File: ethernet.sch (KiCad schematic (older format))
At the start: 31 parts, among them J2 08B0-1X1T-36-F, U6 DP83848JSQ_NOPB, Y1 ABM8G-25.000MHZ-18-D2Y-T

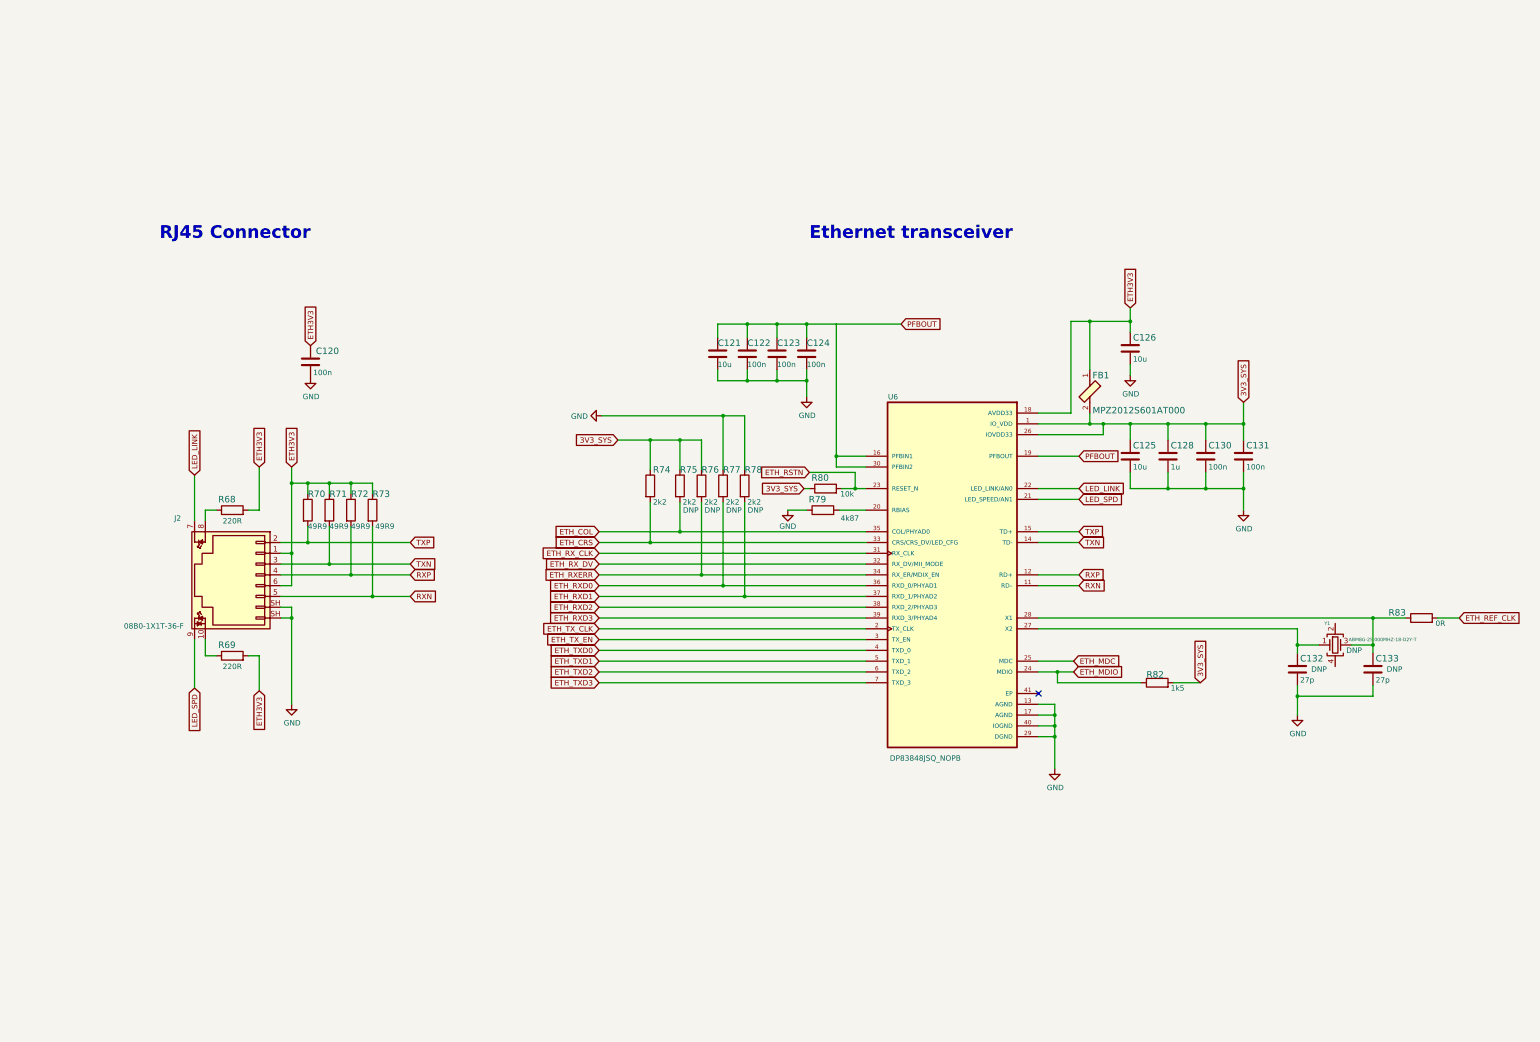
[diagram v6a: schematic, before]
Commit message: Change ETH PHY to KSZ9031RNXCA supporting 1GbE
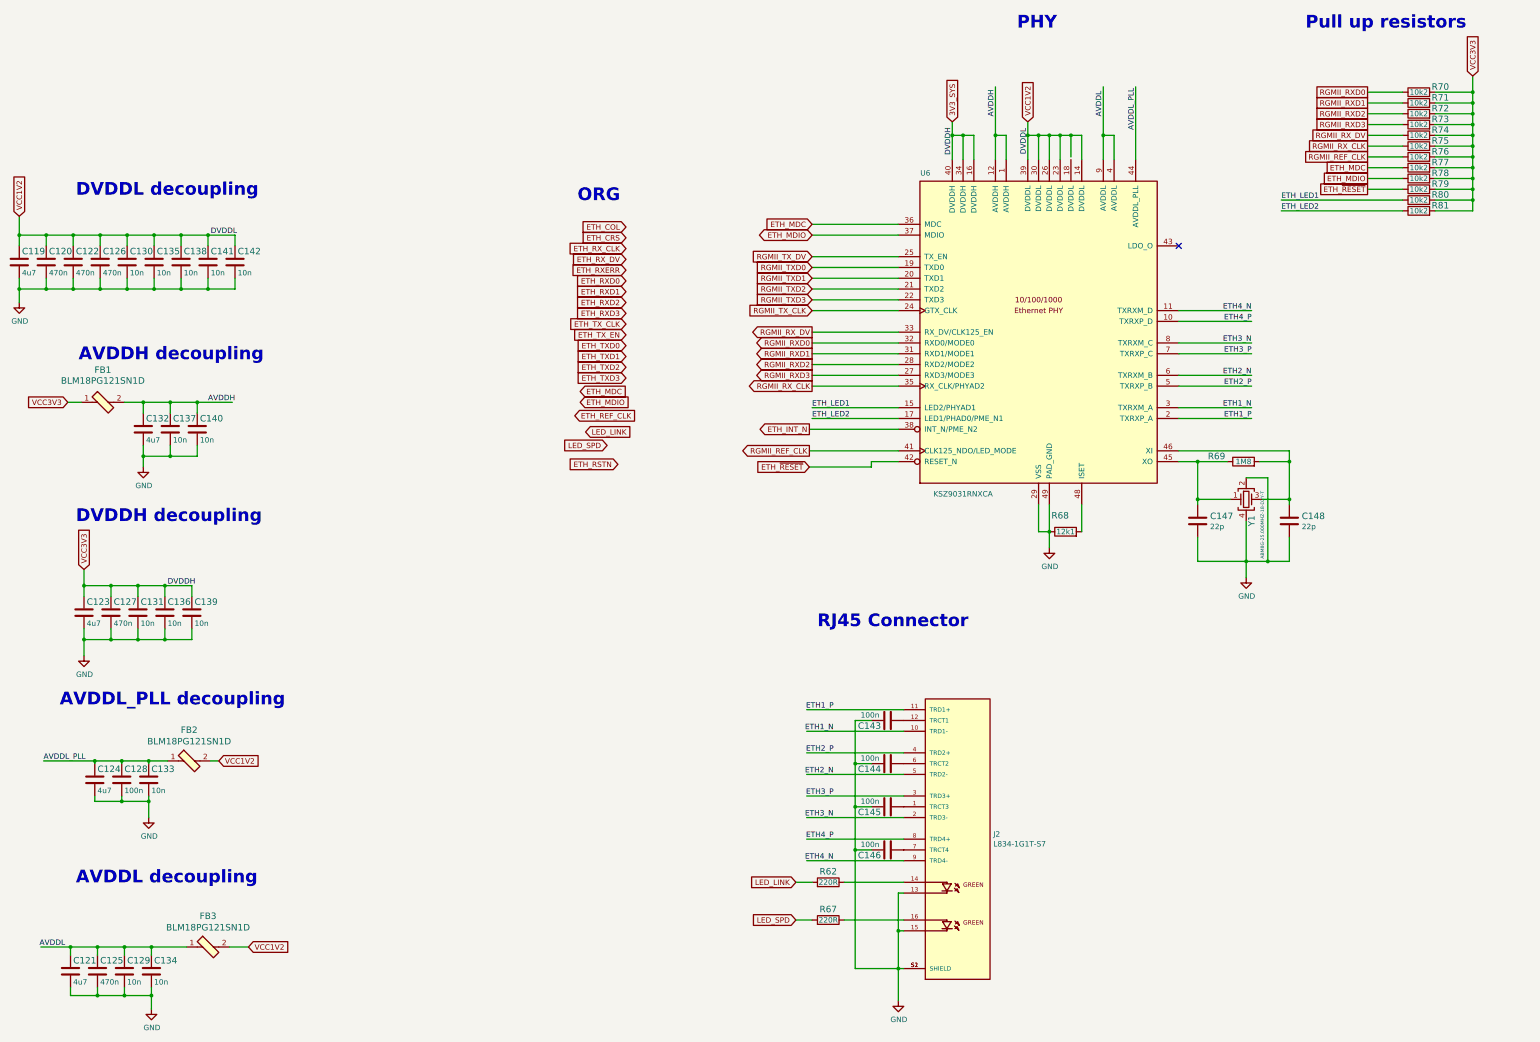
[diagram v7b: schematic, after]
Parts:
- removed C120, C122, C123, C124, C130, C131: C_100n_0402_6V3, lpddr4-test-board-footprints:0402-cap, symbol lpddr4-test-board:C_100n_0402_6V3
- removed C121, C125, C126: C_10u_0603, lpddr4-test-board-footprints:0603-cap, symbol lpddr4-test-board:C_10u_0603
- removed C128: C_1u_0402, lpddr4-test-board-footprints:0402-cap, symbol lpddr4-test-board:C_1u_0402
- removed C132, C133: C_27p_0402, lpddr4-test-board-footprints:0402-cap, symbol lpddr4-test-board:C_27p_0402
- removed FB1: MPZ2012S601AT000, lpddr4-test-board-footprints:0805-res, symbol lpddr4-test-board:MPZ2012S601AT000
- removed J2: 08B0-1X1T-36-F, lpddr4-test-board-footprints:BEL_08B0-1X1T-36-F, symbol lpddr4-test-board:08B0-1X1T-36-F
- removed R68, R69: R_220R_0402, lpddr4-test-board-footprints:0402-res, symbol lpddr4-test-board:R_220R_0402
- removed R70, R71, R72, R73: R_49R9_0402, lpddr4-test-board-footprints:0402-res, symbol lpddr4-test-board:R_49R9_0402
- removed R74, R75, R76, R77, R78: R_2k2_0402, lpddr4-test-board-footprints:0402-res, symbol lpddr4-test-board:R_2k2_0402
- removed R79: R_4k87_0402, lpddr4-test-board-footprints:0402-res, symbol lpddr4-test-board:R_4k87_0402
- removed R80: R_10k_0402, lpddr4-test-board-footprints:0402-res, symbol lpddr4-test-board:R_10k_0402
- removed R82: R_1k5_0402, lpddr4-test-board-footprints:0402-res, symbol lpddr4-test-board:R_1k5_0402
- removed R83: R_0R_0402, lpddr4-test-board-footprints:0402-res, symbol lpddr4-test-board:R_0R_0402
- removed U6: DP83848JSQ_NOPB, lpddr4-test-board-footprints:DP83848JSQ-NOPB, symbol lpddr4-test-board:DP83848JSQ_NOPB
- added C119, C121, C123, C124, C132: C_4u7_0402, artix-dc-scm-footprints:0402-cap, symbol lpddr4-test-board:C_4u7_0402
- added C120, C125, C127: C_470n_0402, artix-dc-scm-footprints:0402-cap, symbol lpddr4-test-board:C_470n_0402
- added C122, C126: C_470n_0402, artix-dc-scm-footprints:0402-cap, symbol antmicroCapacitors0402:C_470n_0402
- added C128, C143, C144, C145, C146: C_100n_0402, artix-dc-scm-footprints:0402-cap, symbol lpddr4-test-board:C_100n_0402_16V
- added C129, C131, C133, C134, C136, C139: C_10n_0402, artix-dc-scm-footprints:0402-cap, symbol lpddr4-test-board:C_10n_0402
- added C130: C_10n_0402, artix-dc-scm-footprints:0402-cap, symbol antmicroCapacitors0402:C_470n_0402
- added C135, C138, C141, C142: C_10n_0402, artix-dc-scm-footprints:0402-cap, symbol antmicroCapacitors0402:C_10n_0402
- added C137: C_10n_0402, artix-dc-scm-footprints:0402-cap, symbol lpddr4-test-board:C_4u7_0402
- added C140: C_10n_0402, artix-dc-scm-footprints:0402-cap, symbol antmicroCapacitors0402:C_4u7_0402
- added C147, C148: C_22p_0402, artix-dc-scm-footprints:0402-cap, symbol antmicroCapacitors0402:C_22p_0402
- added FB1, FB2, FB3: BLM18PG121SN1D, artix-dc-scm-footprints:0603-res, symbol antmicroFerriteBeadsandChips:BLM18PG121SN1D
- added J2: L834-1G1T-S7, artix-dc-scm-footprints:BEL_L834-1G1T-S7, symbol antmicroModularConnectorsJacksWithMagnetics:L834-1G1T-S7
- added R62, R67: R_220R_0402, artix-dc-scm-footprints:0402-res, symbol lpddr4-test-board:R_220R_0402
- added R68: R_12k1_0402, artix-dc-scm-footprints:0402-res, symbol antmicroResistors0402:R_12k1_0402
- added R69: R_1M8_0402, artix-dc-scm-footprints:0402-res, symbol antmicroResistors0402:R_1M8_0402
- added R70, R71, R72, R73, R74, R75, R76, R77, R78, R79, R80, R81: R_10k2_0402, lpddr4-test-board-footprints:0402-res, symbol lpddr4-test-board:R_10k2_0402
- added U6: KSZ9031RNXCA, artix-dc-scm-footprints:QFN-48-Microchip-QFN77-48LD-PL-2, symbol antmicroInterfaceControllers:KSZ9031RNXCA
- Y1: footprint lpddr4-test-board-footprints:KX-7 -> artix-dc-scm-footprints:KX-7; Populate DNP -> (none)
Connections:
- net labels added: AVDDH, AVDDL, AVDDL_PLL, DVDDH, DVDDL, ETH1_N, ETH1_P, ETH2_N, ETH2_P, ETH3_N, ETH3_P, ETH4_N, ETH4_P, ETH_INT_N, ETH_LED1, ETH_LED2, ETH_~RESET, RGMII_REF_CLK, RGMII_RXD0, RGMII_RXD1, RGMII_RXD2, RGMII_RXD3, RGMII_RX_CLK, RGMII_RX_DV, RGMII_TXD0, RGMII_TXD1, RGMII_TXD2, RGMII_TXD3, RGMII_TX_CLK, RGMII_TX_DV, VCC1V2, VCC3V3
- net labels removed: ETH3V3, PFBOUT, RXN, RXP, TXN, TXP
- wire segments 167 -> 246
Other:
- note added: "AVDDH decoupling"
- note added: "AVDDL decoupling"
- note added: "AVDDL_PLL decoupling"
- note added: "DVDDH decoupling"
- note added: "DVDDL decoupling"
- note added: "ORG"
- note added: "PHY"
- note added: "Pull up resistors"
- note removed: "Ethernet transceiver"

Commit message: Connect new PHY signals
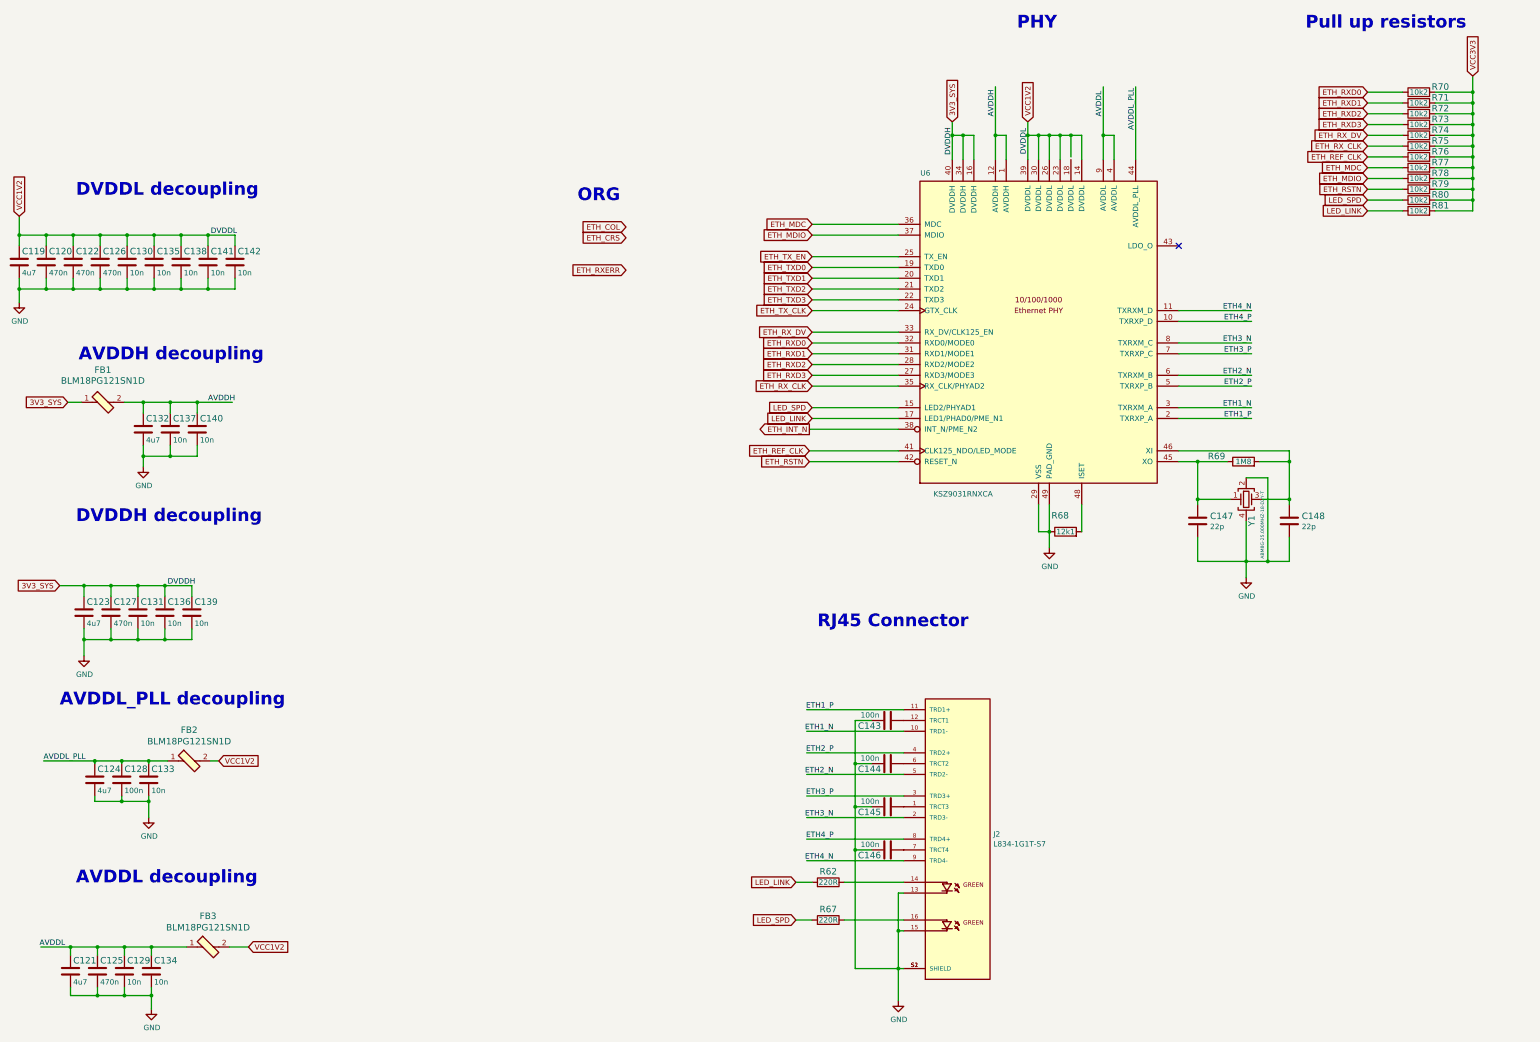
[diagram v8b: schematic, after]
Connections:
- net labels removed: ETH_LED1, ETH_LED2, ETH_~RESET, RGMII_REF_CLK, RGMII_RXD0, RGMII_RXD1, RGMII_RXD2, RGMII_RXD3, RGMII_RX_CLK, RGMII_RX_DV, RGMII_TXD0, RGMII_TXD1, RGMII_TXD2, RGMII_TXD3, RGMII_TX_CLK, RGMII_TX_DV
- wire segments 246 -> 244
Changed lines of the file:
@@
 Wire Wire Line
 	8775 4650 9575 4650
-Text Label 8775 4650 0    50   ~ 0
-ETH_LED1
-Text Label 8775 4750 0    50   ~ 0
-ETH_LED2
 Wire Wire Line
 	9575 4750 8775 4750
@@
 	11275 5550 11275 5800
 NoConn ~ 12175 3150
-Text GLabel 8750 5200 0    50   Input ~ 0
-ETH_~RESET
-Wire Wire Line
-	9575 5150 9325 5150
 Wire Wire Line
 	8750 5050 9575 5050
@@
 Text GLabel 8750 4850 0    50   Output ~ 0
 ETH_INT_N
-Text GLabel 8750 5050 0    50   Output ~ 0
-RGMII_REF_CLK
-Wire Wire Line
-	9325 5150 9325 5200
-Wire Wire Line
-	9325 5200 8750 5200
-Text GLabel 8775 4450 0    50   Output ~ 0
-RGMII_RX_CLK
-Text GLabel 8775 4350 0    50   Output ~ 0
-RGMII_RXD3
-Text GLabel 8775 4250 0    50   Output ~ 0
-RGMII_RXD2
-Text GLabel 8775 4150 0    50   Output ~ 0
-RGMII_RXD1
-Text GLabel 8775 4050 0    50   Output ~ 0
-RGMII_RXD0
 Wire Wire Line
 	8775 4350 9575 4350
@@
 Wire Wire Line
 	9575 4050 8775 4050
-Text GLabel 8775 3750 0    50   Input ~ 0
-RGMII_TX_CLK
-Text GLabel 8775 3650 0    50   Input ~ 0
-RGMII_TXD3
-Text GLabel 8775 3550 0    50   Input ~ 0
-RGMII_TXD2
-Text GLabel 8775 3450 0    50   Input ~ 0
-RGMII_TXD1
-Text GLabel 8775 3350 0    50   Input ~ 0
-RGMII_TXD0
-Text GLabel 8775 3250 0    50   Input ~ 0
-RGMII_TX_DV
 Wire Wire Line
 	8775 3650 9575 3650
@@
 Wire Wire Line
 	9575 3350 8775 3350
-Text GLabel 8775 3050 0    50   BiDi ~ 0
-ETH_MDIO
-Text GLabel 8775 2950 0    50   Input ~ 0
-ETH_MDC
 Wire Wire Line
 	8775 2950 9575 2950
@@
 Wire Wire Line
 	10275 2125 10175 2125
-Text GLabel 8775 3950 0    50   Output ~ 0
-RGMII_RX_DV
 $Comp
 L antmicroInterfaceControllers:KSZ9031RNXCA U?
@@
 	1    0    0    -1
 $EndComp
-Text GLabel 13925 2125 0    50   UnSpc ~ 0
-RGMII_RX_DV
-Text GLabel 13925 2025 0    50   UnSpc ~ 0
-RGMII_RXD3
-Text GLabel 13925 1925 0    50   UnSpc ~ 0
-RGMII_RXD2
-Text GLabel 13925 1725 0    50   UnSpc ~ 0
-RGMII_RXD0
-Text GLabel 13925 1825 0    50   UnSpc ~ 0
-RGMII_RXD1
-Text GLabel 13925 2225 0    50   UnSpc ~ 0
-RGMII_RX_CLK
 Text GLabel 14900 1575 1    50   Input ~ 0
 VCC3V3
-Text GLabel 13925 2325 0    50   UnSpc ~ 0
-RGMII_REF_CLK
-Text GLabel 13925 2525 0    50   UnSpc ~ 0
-ETH_MDIO
-Text GLabel 13925 2425 0    50   UnSpc ~ 0
-ETH_MDC
-Text GLabel 13925 2625 0    50   UnSpc ~ 0
-ETH_~RESET
-Text Label 13125 2725 0    50   ~ 0
-ETH_LED1
-Text Label 13125 2825 0    50   ~ 0
-ETH_LED2
 Text Notes 13350 1150 0    118  ~ 24
 Pull up resistors
@@
 	13925 2625 14250 2625
 Wire Wire Line
-	14250 2725 13125 2725
-Wire Wire Line
-	13125 2825 14250 2825
-Text GLabel 7050 4075 0    50   Input ~ 0
+	14250 2725 13925 2725
+Wire Wire Line
+	13925 2825 14250 2825
+Text GLabel 8775 3350 0    50   Input ~ 0
 ETH_TXD0
-Text GLabel 7050 4175 0    50   Input ~ 0
+Text GLabel 8775 3450 0    50   Input ~ 0
 ETH_TXD1
-Text GLabel 7050 4275 0    50   Input ~ 0
+Text GLabel 8775 3550 0    50   Input ~ 0
 ETH_TXD2
-Text GLabel 7050 4375 0    50   Input ~ 0
+Text GLabel 8775 3650 0    50   Input ~ 0
 ETH_TXD3
-Text GLabel 7050 3875 0    50   Input ~ 0
+Text GLabel 8775 3750 0    50   Input ~ 0
 ETH_TX_CLK
-Text GLabel 7050 3975 0    50   Input ~ 0
+Text GLabel 8775 3250 0    50   Input ~ 0
 ETH_TX_EN
-Text GLabel 7050 3475 0    50   Input ~ 0
+Text GLabel 8775 4050 0    50   Input ~ 0
 ETH_RXD0
-Text GLabel 7050 3575 0    50   Input ~ 0
+Text GLabel 8775 4150 0    50   Input ~ 0
 ETH_RXD1
-Text GLabel 7050 3675 0    50   Input ~ 0
+Text GLabel 8775 4250 0    50   Input ~ 0
 ETH_RXD2
-Text GLabel 7050 3775 0    50   Input ~ 0
+Text GLabel 8775 4350 0    50   Input ~ 0
 ETH_RXD3
-Text GLabel 7050 3175 0    50   Input ~ 0
+Text GLabel 8775 4450 0    50   Input ~ 0
 ETH_RX_CLK
-Text GLabel 7050 3275 0    50   Input ~ 0
+Text GLabel 8775 3950 0    50   Input ~ 0
 ETH_RX_DV
 Text GLabel 7050 3375 0    50   Input ~ 0
@@
 Text GLabel 7050 3075 0    50   Input ~ 0
 ETH_CRS
-Text GLabel 6625 4500 2    50   Input ~ 0
+Text GLabel 8775 2950 0    50   Input ~ 0
 ETH_MDC
-Text GLabel 6625 4600 2    50   Input ~ 0
+Text GLabel 8775 3050 0    50   Input ~ 0
 ETH_MDIO
 Text Notes 6600 2750 0    118  ~ 24
@@
 Text GLabel 10075 2000 1    50   Input ~ 0
 3V3_SYS
-Text GLabel 6575 4725 2    50   Input ~ 0
+Text GLabel 8750 5050 0    50   Input ~ 0
 ETH_REF_CLK
-Text GLabel 6675 4875 2    50   Input ~ 0
+Text GLabel 8775 4750 0    50   Input ~ 0
 LED_LINK
-Text GLabel 6875 5000 0    50   Input ~ 0
+Text GLabel 8775 4650 0    50   Input ~ 0
 LED_SPD
-Text GLabel 6975 5175 0    50   Input ~ 0
+Text GLabel 8750 5150 0    50   Input ~ 0
 ETH_RSTN
 Text GLabel 8625 9400 0    50   Input ~ 0
@@
 Wire Wire Line
 	1425 3550 1425 3675
-Text GLabel 2025 6150 1    50   Input ~ 0
-VCC3V3
-Text GLabel 1875 4600 0    50   Input ~ 0
-VCC3V3
 Wire Wire Line
 	2575 5100 2825 5100
@@
 Connection ~ 2025 6800
 Wire Wire Line
-	2025 6150 2025 6300
+	1800 6300 2025 6300
 Connection ~ 2025 6300
 Text Notes 1950 5725 0    118  ~ 24
@@
 	1    0    0    -1
 $EndComp
+Text GLabel 1875 4600 0    50   Input ~ 0
+3V3_SYS
+Text GLabel 1800 6300 0    50   Input ~ 0
+3V3_SYS
+Wire Wire Line
+	8750 5150 9575 5150
+Text GLabel 13925 1725 0    50   Input ~ 0
+ETH_RXD0
+Text GLabel 13925 1825 0    50   Input ~ 0
+ETH_RXD1
+Text GLabel 13925 1925 0    50   Input ~ 0
+ETH_RXD2
+Text GLabel 13925 2025 0    50   Input ~ 0
+ETH_RXD3
+Text GLabel 13925 2225 0    50   Input ~ 0
+ETH_RX_CLK
+Text GLabel 13925 2125 0    50   Input ~ 0
+ETH_RX_DV
+Text GLabel 13925 2425 0    50   Input ~ 0
+ETH_MDC
+Text GLabel 13925 2525 0    50   Input ~ 0
+ETH_MDIO
+Text GLabel 13925 2325 0    50   Input ~ 0
+ETH_REF_CLK
+Text GLabel 13925 2625 0    50   Input ~ 0
+ETH_RSTN
+Text GLabel 13925 2825 0    50   Input ~ 0
+LED_LINK
+Text GLabel 13925 2725 0    50   Input ~ 0
+LED_SPD
 $EndSCHEMATC
